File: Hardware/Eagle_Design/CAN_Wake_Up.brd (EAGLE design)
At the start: 50 x 50 mm, 35 parts, among them IC1 STM32F10XCXT6, IC4 LM1117MP-5.0, IC5 LM1117MP-3.3, Q1 8MHz

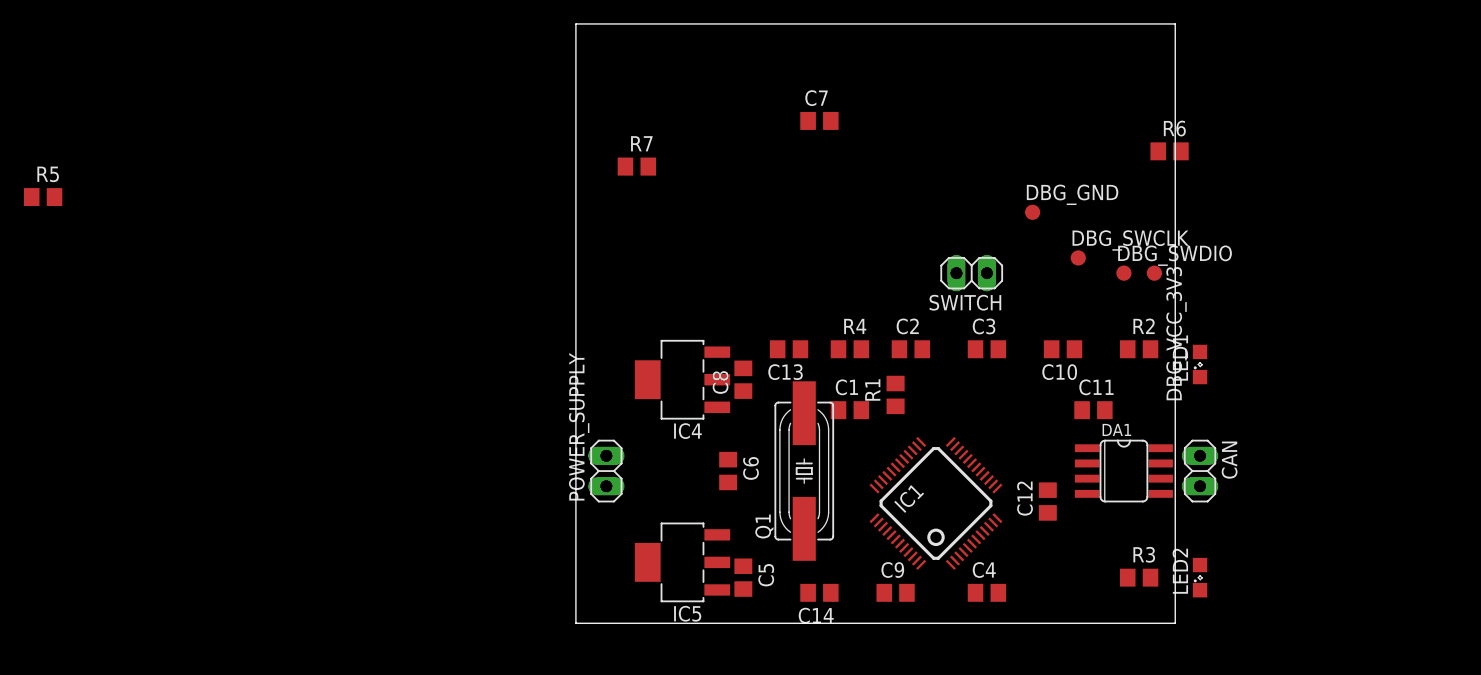
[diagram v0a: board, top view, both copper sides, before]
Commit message: Continued on layout. Not yet fully routable. PCB need to be resized.
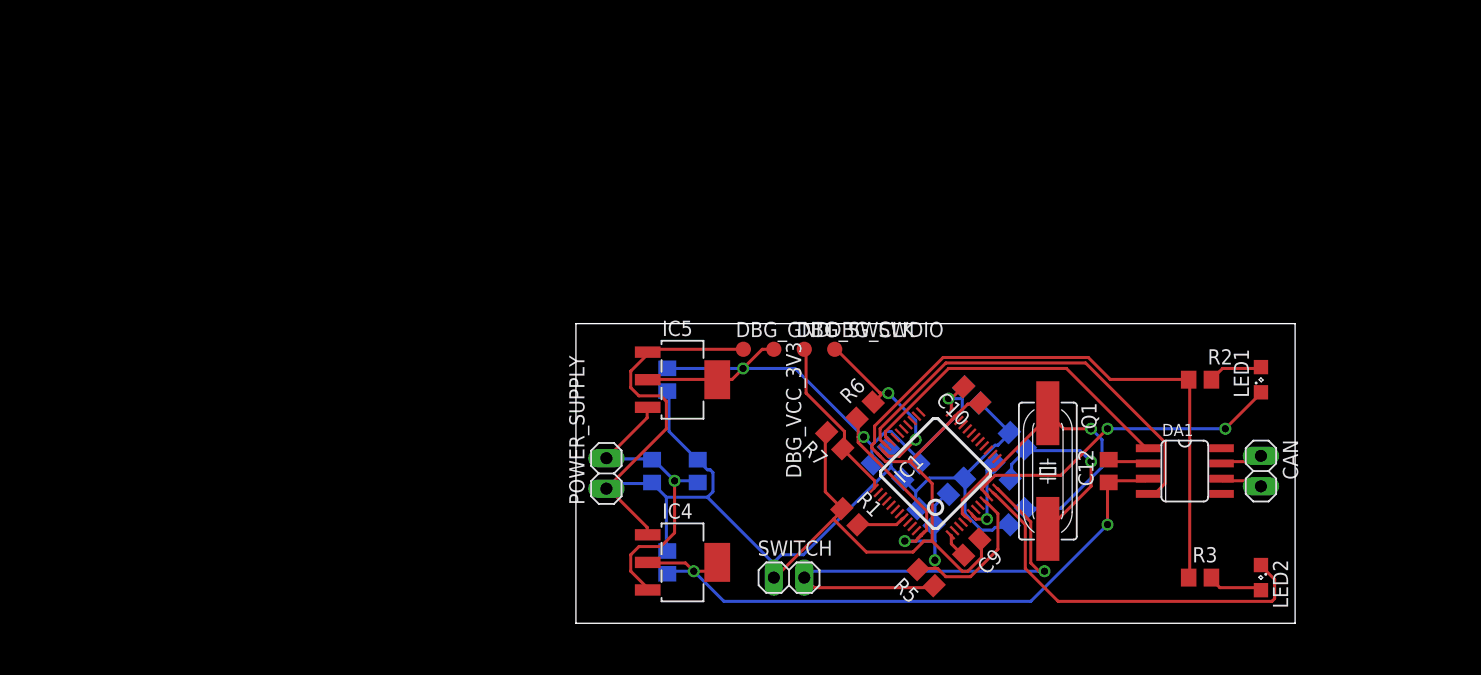
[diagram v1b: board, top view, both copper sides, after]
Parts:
- moved R5 80.2 mm to (29.2, 3.81), turned to 135 degrees
- moved C7 39.0 mm to (7.62, 5.08), flipped to the bottom, turned to 90 degrees
- moved R6 33.3 mm to (24.1, 17.8), turned to 45 degrees
- moved DBG_VCC_3V3 32.4 mm to (16.5, 22.9)
- moved SWITCH 29.6 mm to (17.8, 3.81), turned to 0 degrees
- moved R7 28.2 mm to (21.6, 15.2), turned to 135 degrees
- moved DBG_GND 26.7 mm to (14.0, 22.9)
- moved DBG_SWDIO 25.0 mm to (21.6, 22.9)
- moved DBG_SWCLK 24.1 mm to (19.1, 22.9)
- moved C13 20.5 mm to (36.8, 15.2), flipped to the bottom, turned to 225 degrees
- moved Q1 20.3 mm to (39.4, 12.7), turned to 270 degrees
- moved C14 17.7 mm to (36.8, 8.89), flipped to the bottom, turned to 135 degrees
- moved R4 16.3 mm to (35.6, 12.7), flipped to the bottom, turned to 45 degrees
- moved IC4 15.2 mm to (8.89, 5.08), turned to 270 degrees
- moved IC5 15.2 mm to (8.89, 20.3), turned to 270 degrees
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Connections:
- new net CAN_S_MCU: DA1.8, IC1.31
- net GND: no longer DA1.8
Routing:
- net GND: track 0.00 -> 203.7 mm
- net VCC_3V3: track 0.00 -> 87.0 mm, vias 0 -> 5
- net VCC_5V: track 0.00 -> 53.9 mm, vias 0 -> 2
- net SW_MCU_CAN: track 0.00 -> 40.3 mm, vias 0 -> 1
- net CAN_TX_MCU: track 0.00 -> 35.7 mm
- net LED_MCU_CAN: track 0.00 -> 32.8 mm
- net CAN_RX_MCU: track 0.00 -> 27.9 mm
- net LED_MCU_PWR: track 0.00 -> 27.6 mm, vias 0 -> 2
- net N$6: track 0.00 -> 27.5 mm, vias 0 -> 1
- net KL30: track 0.00 -> 26.4 mm, vias 0 -> 1
- net N$5: track 0.00 -> 16.1 mm, vias 0 -> 1
- net DBG_SWDIO: track 0.00 -> 15.5 mm, vias 0 -> 2
- net DBG_SWCLK: track 0.00 -> 14.3 mm
- net N$7: track 0.00 -> 6.45 mm, vias 0 -> 1
- net N$4: track 0.00 -> 4.76 mm
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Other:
- board size 50 x 50 mm -> 60 x 25 mm

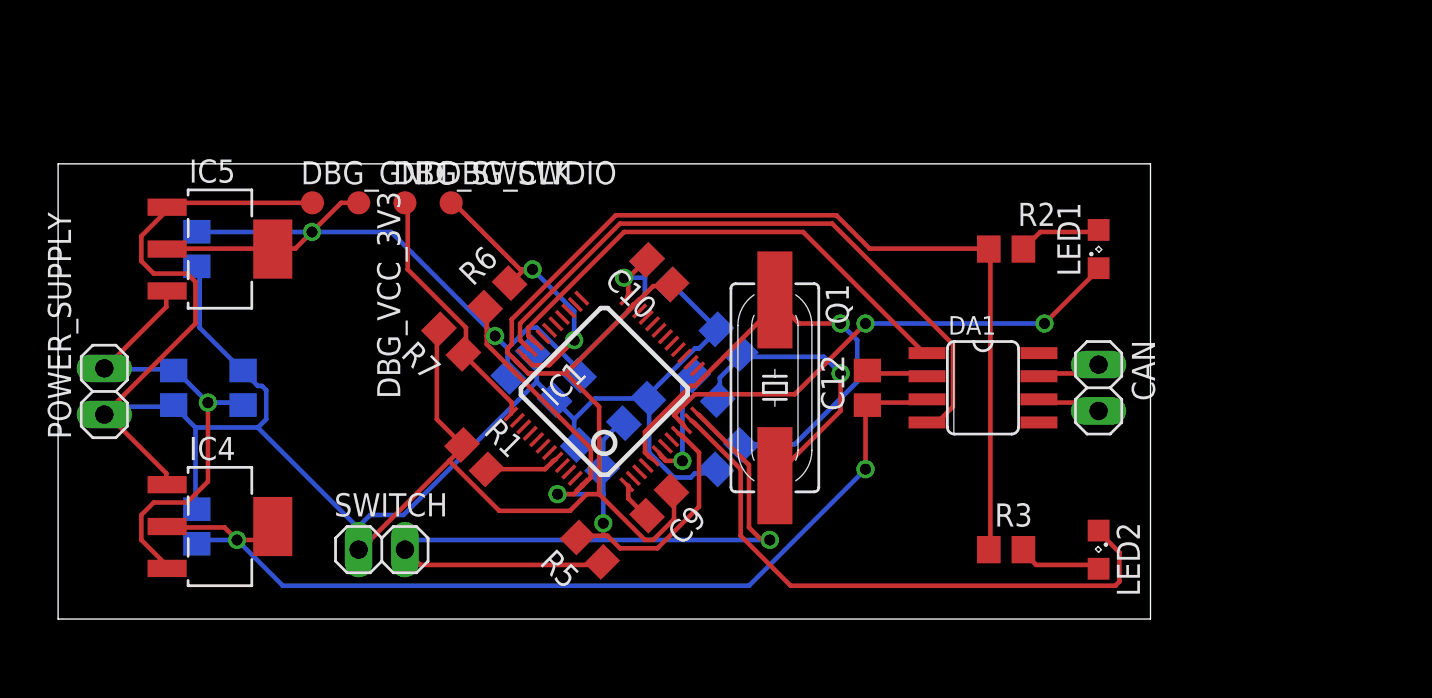
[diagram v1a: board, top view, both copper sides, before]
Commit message: Finished board layout. First order at seeedstudio.com
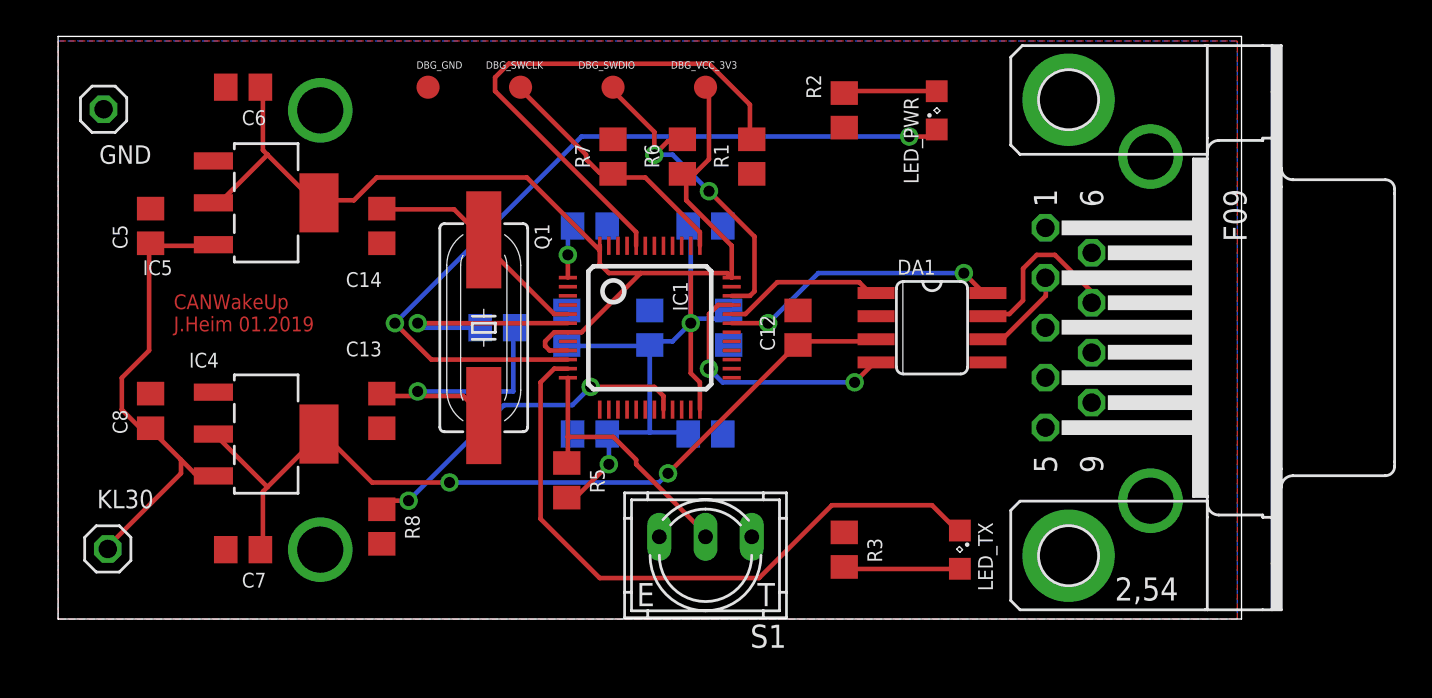
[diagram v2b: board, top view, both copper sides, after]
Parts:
- removed CAN, POWER_SUPPLY, SWITCH: (no value), pinhead:1X02
- removed LED1: RED, led:SML0805
- removed LED2: GREEN, led:SML0805
- added DSUB-9: CAN, con-subd:F09HP
- added GND, KL30: (no value), pinhead:1X01
- added H1, H2, H3, H4: SPECIAL_DRILL_0.1000, special-drill:PAD_0.1000
- added LED_PWR: RED, led:SML0805
- added LED_TX: GREEN, led:SML0805
- added R8: 10k, rcl:R0805
- added S1: 9077-1, switch-misc:9077-1
- moved C14 22.9 mm to (17.8, 21.6), flipped to the top, turned to 90 degrees
- moved R1 22.5 mm to (38.1, 25.4), turned to 90 degrees
- moved DBG_VCC_3V3 20.1 mm to (35.6, 29.2)
- moved C13 19.4 mm to (17.8, 11.4), flipped to the top, turned to 90 degrees
- moved Q1 16.3 mm to (23.4, 16.0)
- moved C9 15.7 mm to (29.2, 21.6), flipped to the bottom, turned to 0 degrees
- moved R7 13.5 mm to (30.5, 25.4), turned to 90 degrees
- moved R6 12.7 mm to (34.3, 25.4), turned to 90 degrees
- moved R4 11.9 mm to (24.1, 16.0), turned to 0 degrees
- moved R2 11.7 mm to (43.2, 27.9), turned to 90 degrees
- moved DBG_SWDIO 10.9 mm to (30.5, 29.2), turned to 270 degrees
- moved C6 9.25 mm to (10.2, 29.2), flipped to the top, turned to 180 degrees
- moved C5 8.98 mm to (5.08, 21.6), flipped to the top, turned to 90 degrees
- moved DBG_GND 8.98 mm to (20.3, 29.2), turned to 270 degrees
- moved DBG_SWCLK 8.98 mm to (25.4, 29.2), turned to 270 degrees
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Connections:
- removed net KL31: C12.2, DA1.2
- new net N$8: IC1.20, R8.1
- net CAN_H: now also DSUB-9.7; no longer CAN.1
- net CAN_L: now also DSUB-9.2; no longer CAN.2
- net GND: now also C12.2, DA1.2, DSUB-9.3, DSUB-9.G1, GND.1, H1.1, H2.1, H3.1, H4.1, R8.2, S1.1; no longer POWER_SUPPLY.1, SWITCH.1
- net KL30: now also KL30.1; no longer POWER_SUPPLY.2
- net LED_MCU_CAN: now also LED_TX.C; no longer LED2.C
- net LED_MCU_PWR: now also LED_PWR.C; no longer LED1.C
- net N$3: now also LED_PWR.A; no longer LED1.A
- net N$4: now also LED_TX.A; no longer LED2.A
- net SW_MCU_CAN: now also S1.2; no longer SWITCH.2
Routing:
- net GND: track 203.7 -> 0.00 mm
- net N$1: track 4.04 -> 29.6 mm
- net SW_MCU_CAN: track 40.3 -> 14.8 mm, vias 1 -> 0
- net CAN_TX_MCU: track 35.7 -> 14.4 mm, vias 0 -> 2
- net N$8: track 0.00 -> 19.2 mm, vias 0 -> 2
- net CAN_RX_MCU: track 27.9 -> 9.02 mm
- net LED_MCU_PWR: track 27.6 -> 44.6 mm
- net CAN_S_MCU: track 0.00 -> 15.8 mm, vias 0 -> 2
- net N$6: track 27.5 -> 12.9 mm, vias 1 -> 0
- net VCC_3V3: track 87.0 -> 96.5 mm, vias 5 -> 2
- net VCC_5V: track 53.9 -> 46.8 mm
- net CAN_H: track 3.59 -> 9.54 mm
- net N$7: track 6.45 -> 11.8 mm
- net KL31: track 3.41 -> 0.00 mm
- net LED_MCU_CAN: track 32.8 -> 36.0 mm
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- added copper zone on layer 1, net GND
- added copper zone on layer 16, net GND
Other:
- board size 60 x 25 mm -> 65 x 32 mm
- board text added: "CANWakeUp J.Heim 01.2019"

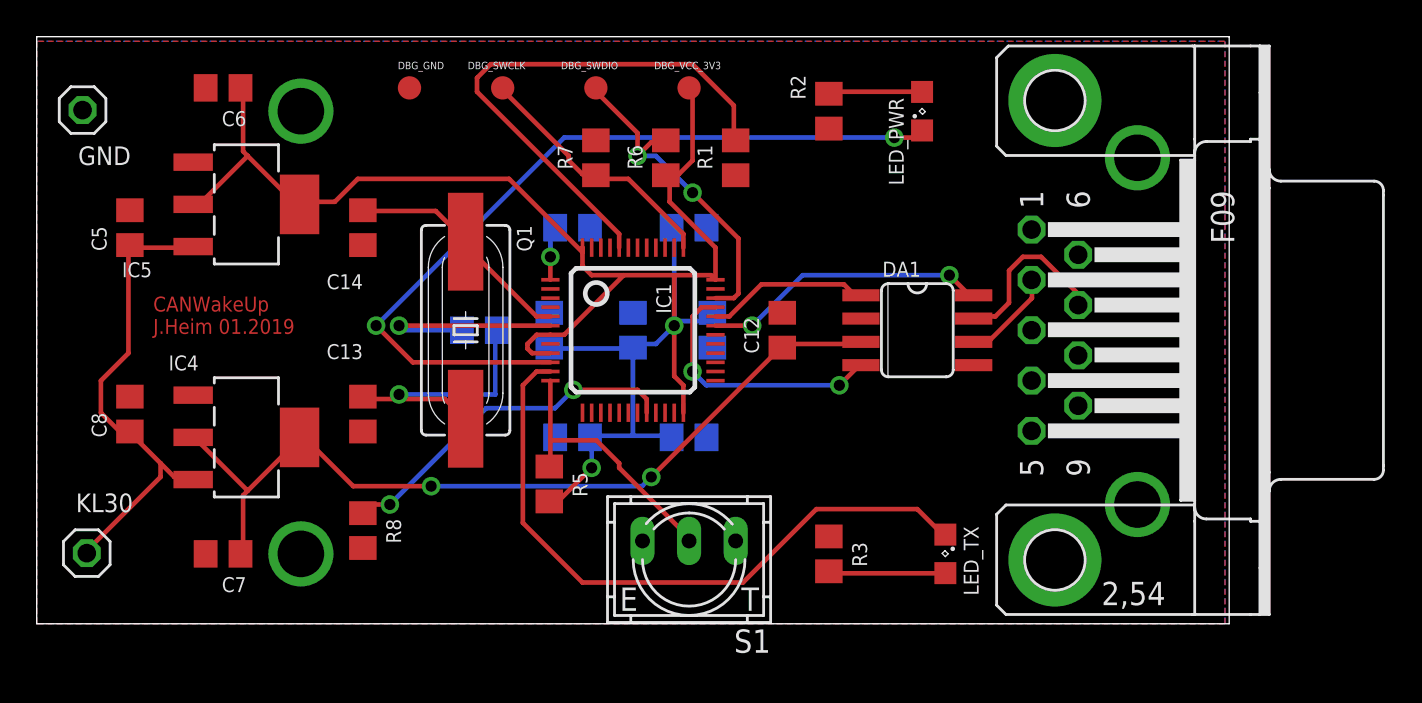
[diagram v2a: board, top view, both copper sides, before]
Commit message: New version. Added Eagle BOM (.csv) file.
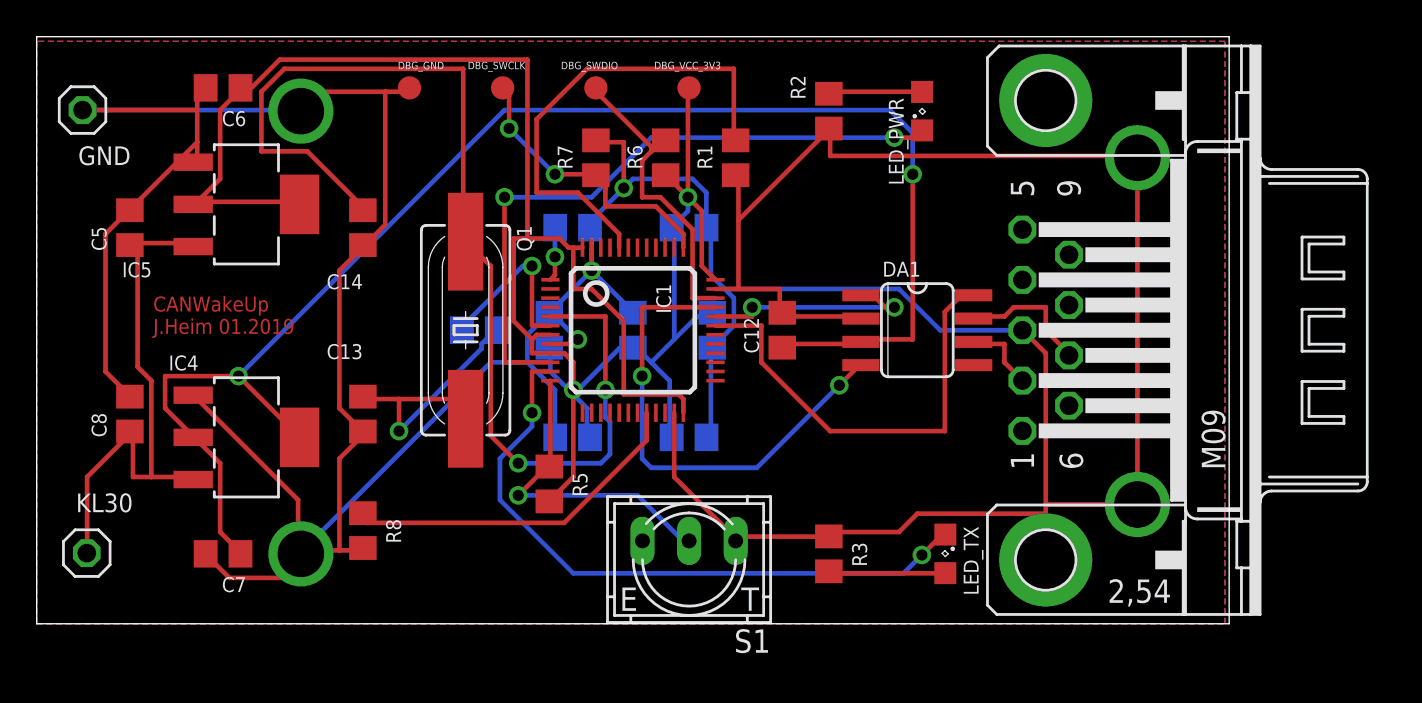
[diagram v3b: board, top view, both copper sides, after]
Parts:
- DSUB-9: device con-subd:F09HP -> con-subd:M09HP
- moved DSUB-9 0.50 mm to (55.0, 16.0), turned to 90 degrees
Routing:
- net GND: track 0.00 -> 284.1 mm, vias 0 -> 3
- net N$6: track 12.9 -> 60.3 mm, vias 0 -> 2
- net VCC_5V: track 46.8 -> 82.0 mm
- net VCC_3V3: track 96.5 -> 117.6 mm
- net CAN_TX_MCU: track 14.4 -> 26.7 mm
- net CAN_S_MCU: track 15.8 -> 24.5 mm, vias 2 -> 0
- net LED_MCU_PWR: track 44.6 -> 36.0 mm
- net KL30: track 26.5 -> 30.3 mm
- net N$1: track 29.6 -> 26.0 mm
- net CAN_RX_MCU: track 9.02 -> 12.4 mm, vias 0 -> 2
- net SW_MCU_CAN: track 14.8 -> 17.4 mm, vias 0 -> 1
- net CAN_H: track 9.54 -> 7.31 mm
- net N$7: track 11.8 -> 9.88 mm
- net DBG_SWCLK: track 14.2 -> 15.6 mm, vias 0 -> 2
- net DBG_SWDIO: track 18.3 -> 17.1 mm, vias 2 -> 0
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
